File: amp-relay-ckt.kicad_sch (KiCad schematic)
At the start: 15 parts, among them K1 HK19F-DCxxV-SHC, K11 HK19F-DCxxV-SHC, Q2 Q_PNP_BCE, Q5 BSS123, U1 LM7805_TO220

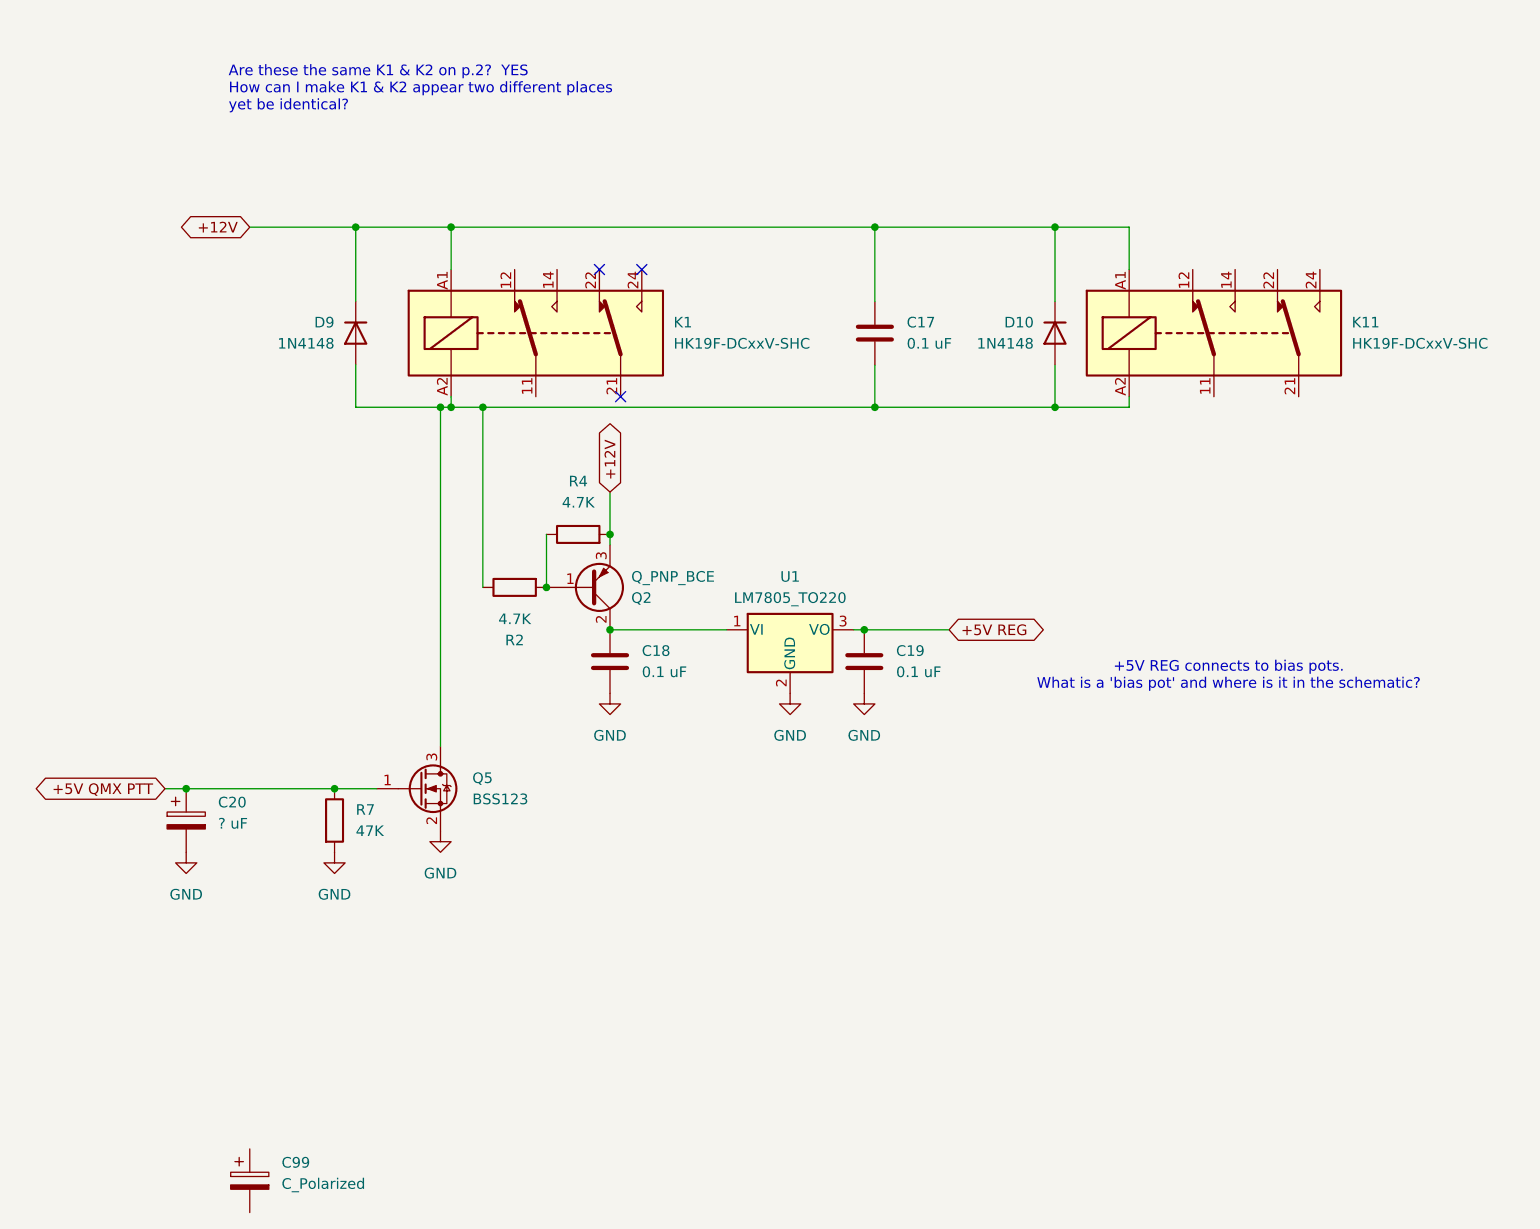
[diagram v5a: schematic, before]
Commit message: changed +5V and +12V from global symbol to the more normal voltage busses
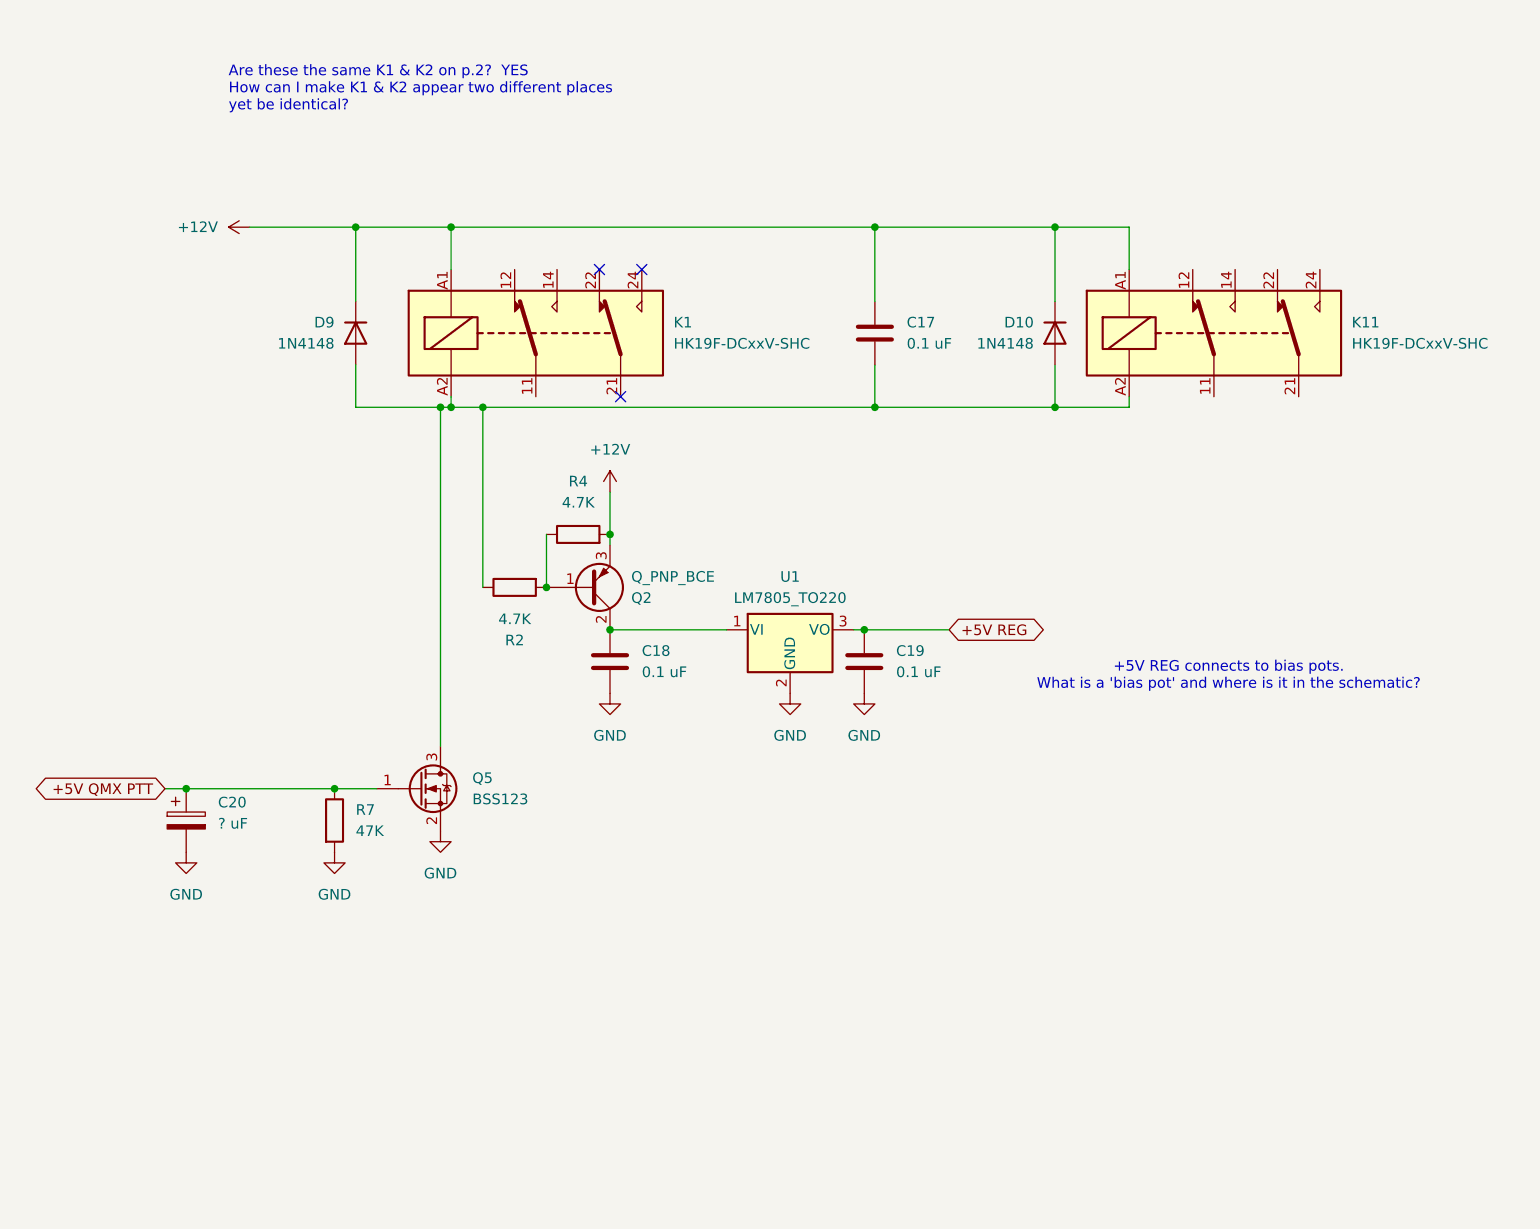
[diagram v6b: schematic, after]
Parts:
- removed C99: C_Polarized, symbol Device:C_Polarized
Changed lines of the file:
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@@
 		)
 	)
-	(global_label "+12V"
+	(global_label "+5V REG"
 		(shape bidirectional)
-		(at 102.87 85.09 90)
+		(at 143.51 101.6 0)
 		(fields_autoplaced yes)
 		(effects
@@
 		)
 		(property "Intersheetrefs" "${INTERSHEET_REFS}"
-			(at 102.87 75.9137 90)
-			(effects
-				(font
-					(size 1.27 1.27)
-				)
-				(justify left)
-				(hide yes)
-			)
-		)
-	)
-	(global_label "+5V REG"
+			(at 156.1334 101.6 0)
+			(effects
+				(font
+					(size 1.27 1.27)
+				)
+				(justify left)
+				(hide yes)
+			)
+		)
+	)
+	(global_label "+5V QMX PTT"
 		(shape bidirectional)
-		(at 143.51 101.6 0)
+		(at 49.53 120.65 180)
 		(fields_autoplaced yes)
 		(effects
@@
 				(size 1.27 1.27)
 			)
-			(justify left)
-		)
-		(property "Intersheetrefs" "${INTERSHEET_REFS}"
-			(at 156.1334 101.6 0)
-			(effects
-				(font
-					(size 1.27 1.27)
-				)
-				(justify left)
-				(hide yes)
-			)
-		)
-	)
-	(global_label "+5V QMX PTT"
-		(shape bidirectional)
-		(at 49.53 120.65 180)
-		(fields_autoplaced yes)
-		(effects
-			(font
-				(size 1.27 1.27)
-			)
 			(justify right)
 		)
@@
 				(justify right)
 				(hide yes)
-			)
-		)
-	)
-	(global_label "+12V"
-		(shape bidirectional)
-		(at 59.69 53.34 180)
-		(fields_autoplaced yes)
-		(effects
-			(font
-				(size 1.27 1.27)
-			)
-			(justify right)
-		)
-		(property "Intersheetrefs" "${INTERSHEET_REFS}"
-			(at 50.5137 53.34 0)
-			(effects
-				(font
-					(size 1.27 1.27)
-				)
-				(justify right)
-				(hide yes)
-			)
-		)
-	)
-	(symbol
-		(lib_id "Device:C_Polarized")
-		(at 59.69 167.64 0)
-		(unit 1)
-		(exclude_from_sim no)
-		(in_bom yes)
-		(on_board yes)
-		(dnp no)
-		(fields_autoplaced yes)
-		(property "Reference" "C99"
-			(at 63.5 165.4809 0)
-			(effects
-				(font
-					(size 1.27 1.27)
-				)
-				(justify left)
-			)
-		)
-		(property "Value" "C_Polarized"
-			(at 63.5 168.0209 0)
-			(effects
-				(font
-					(size 1.27 1.27)
-				)
-				(justify left)
-			)
-		)
-		(property "Footprint" ""
-			(at 60.6552 171.45 0)
-			(effects
-				(font
-					(size 1.27 1.27)
-				)
-				(hide yes)
-			)
-		)
-		(property "Datasheet" "~"
-			(at 59.69 167.64 0)
-			(effects
-				(font
-					(size 1.27 1.27)
-				)
-				(hide yes)
-			)
-		)
-		(property "Description" "Polarized capacitor"
-			(at 59.69 167.64 0)
-			(effects
-				(font
-					(size 1.27 1.27)
-				)
-				(hide yes)
-			)
-		)
-		(pin "2"
-		)
-		(pin "1"
-		)
-		(instances
-			(project ""
-				(path "/e63e39d7-6ac0-4ffd-8aa3-1841a4541b55/6e8a5723-6162-4126-acdf-190058cf1f27"
-					(reference "C99")
-					(unit 1)
-				)
 			)
 		)
@@
 	)
 	(symbol
+		(lib_id "power:+12V")
+		(at 59.69 53.34 90)
+		(unit 1)
+		(exclude_from_sim no)
+		(in_bom yes)
+		(on_board yes)
+		(dnp no)
+		(fields_autoplaced yes)
+		(property "Reference" "#PWR032"
+			(at 63.5 53.34 0)
+			(effects
+				(font
+					(size 1.27 1.27)
+				)
+				(hide yes)
+			)
+		)
+		(property "Value" "+12V"
+			(at 55.88 53.3399 90)
+			(effects
+				(font
+					(size 1.27 1.27)
+				)
+				(justify left)
+			)
+		)
+		(property "Footprint" ""
+			(at 59.69 53.34 0)
+			(effects
+				(font
+					(size 1.27 1.27)
+				)
+				(hide yes)
+			)
+		)
+		(property "Datasheet" ""
+			(at 59.69 53.34 0)
+			(effects
+				(font
+					(size 1.27 1.27)
+				)
+				(hide yes)
+			)
+		)
+		(property "Description" "Power symbol creates a global label with name \"+12V\""
+			(at 59.69 53.34 0)
+			(effects
+				(font
+					(size 1.27 1.27)
+				)
+				(hide yes)
+			)
+		)
+		(pin "1"
+		)
+		(instances
+			(project ""
+				(path "/e63e39d7-6ac0-4ffd-8aa3-1841a4541b55/6e8a5723-6162-4126-acdf-190058cf1f27"
+					(reference "#PWR032")
+					(unit 1)
+				)
+			)
+		)
+	)
+	(symbol
 		(lib_id "Device:D")
 		(at 72.39 66.04 90)
@@
 					(unit 1)
 				)
+			)
+		)
+	)
+	(symbol
+		(lib_id "power:+12V")
+		(at 102.87 85.09 0)
+		(unit 1)
+		(exclude_from_sim no)
+		(in_bom yes)
+		(on_board yes)
+		(dnp no)
+		(fields_autoplaced yes)
+		(property "Reference" "#PWR031"
+			(at 102.87 88.9 0)
+			(effects
+				(font
+					(size 1.27 1.27)
+				)
+				(hide yes)
+			)
+		)
+		(property "Value" "+12V"
+			(at 102.87 80.01 0)
+			(effects
+				(font
+					(size 1.27 1.27)
+				)
+			)
+		)
+		(property "Footprint" ""
+			(at 102.87 85.09 0)
+			(effects
+				(font
+					(size 1.27 1.27)
+				)
+				(hide yes)
+			)
+		)
+		(property "Datasheet" ""
+			(at 102.87 85.09 0)
+			(effects
+				(font
+					(size 1.27 1.27)
+				)
+				(hide yes)
+			)
+		)
+		(property "Description" "Power symbol creates a global label with name \"+12V\""
+			(at 102.87 85.09 0)
+			(effects
+				(font
+					(size 1.27 1.27)
+				)
+				(hide yes)
+			)
+		)
+		(pin "1"
+		)
+		(instances
+			(project ""
+				(path "/e63e39d7-6ac0-4ffd-8aa3-1841a4541b55/6e8a5723-6162-4126-acdf-190058cf1f27"
+					(reference "#PWR031")
+					(unit 1)
+				)

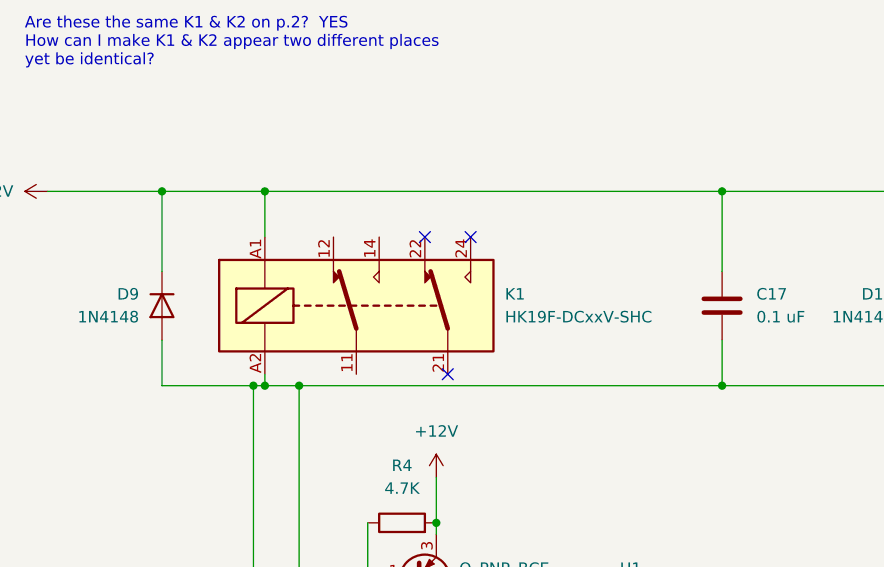
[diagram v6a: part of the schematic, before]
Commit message: could not figure out how to have two instances of K1 so I used global labels.  STINKY HACK
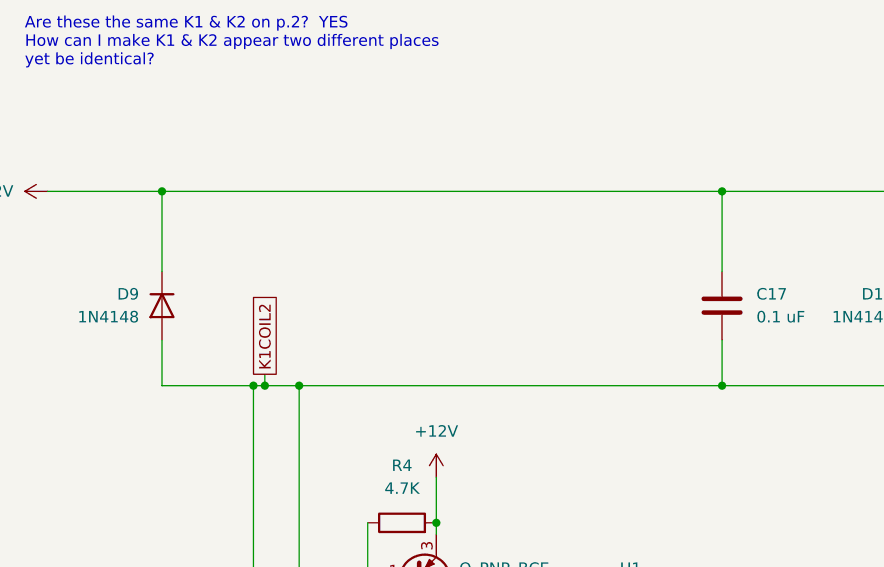
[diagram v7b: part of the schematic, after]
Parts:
- removed K1: HK19F-DCxxV-SHC, Relay_THT:Relay_DPDT_Finder_30.22, symbol Relay:HK19F-DCxxV-SHC
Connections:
- net K1COIL2: now reaches C17.2, D10.2 (A), D9.2 (A), K11.A2, Q5.3 (D), R2.1
- no-connect marks 3 -> 0
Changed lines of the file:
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@@
-	)
-	(junction
-		(at 83.82 53.34)
-		(diameter 0)
-		(color 0 0 0 0)
 	)
 	(junction
@@
 		(color 0 0 0 0)
 	)
-	(no_connect
-		(at 101.6 58.42)
-	)
-	(no_connect
-		(at 106.68 58.42)
-	)
-	(no_connect
-		(at 104.14 73.66)
-	)
 	(wire
 		(pts
@@
 	(wire
 		(pts
-			(xy 72.39 53.34) (xy 83.82 53.34)
+			(xy 72.39 53.34) (xy 134.62 53.34)
 		)
 		(stroke
@@
 	(wire
 		(pts
-			(xy 83.82 53.34) (xy 83.82 58.42)
-		)
-		(stroke
-			(width 0)
-			(type default)
-		)
-	)
-	(wire
-		(pts
 			(xy 133.35 101.6) (xy 132.08 101.6)
 		)
@@
 		(pts
 			(xy 83.82 73.66) (xy 83.82 74.93)
-		)
-		(stroke
-			(width 0)
-			(type default)
-		)
-	)
-	(wire
-		(pts
-			(xy 83.82 53.34) (xy 134.62 53.34)
 		)
 		(stroke
@@
 		)
 	)
+	(global_label "K1COIL2"
+		(shape passive)
+		(at 83.82 73.66 90)
+		(fields_autoplaced yes)
+		(effects
+			(font
+				(size 1.27 1.27)
+			)
+			(justify left)
+		)
+		(property "Intersheetrefs" "${INTERSHEET_REFS}"
+			(at 83.82 63.6733 90)
+			(effects
+				(font
+					(size 1.27 1.27)
+				)
+				(justify left)
+				(hide yes)
+			)
+		)
+	)
 	(global_label "+5V QMX PTT"
 		(shape bidirectional)
@@
 					(unit 1)
 				)
-			)
-		)
-	)
-	(symbol
-		(lib_id "Relay:HK19F-DCxxV-SHC")
-		(at 93.98 66.04 0)
-		(unit 1)
-		(exclude_from_sim no)
-		(in_bom yes)
-		(on_board yes)
-		(dnp no)
-		(fields_autoplaced yes)
-		(property "Reference" "K1"
-			(at 110.49 64.7699 0)
-			(effects
-				(font
-					(size 1.27 1.27)
-				)
-				(justify left)
-			)
-		)
-		(property "Value" "HK19F-DCxxV-SHC"
-			(at 110.49 67.3099 0)
-			(effects
-				(font
-					(size 1.27 1.27)
-				)
-				(justify left)
-			)
-		)
-		(property "Footprint" "Relay_THT:Relay_DPDT_Finder_30.22"
-			(at 76.2 78.74 0)
-			(effects
-				(font
-					(size 1.27 1.27)
-				)
-				(justify left)
-				(hide yes)
-			)
-		)
-		(property "Datasheet" "https://www.lcsc.com/datasheet/lcsc_datasheet_1810201512_Ningbo-Keke-New-Era-Appliance-HK19F-DC12V-SHG_C42803.pdf"
-			(at 93.98 83.82 0)
-			(effects
-				(font
-					(size 1.27 1.27)
-				)
-				(hide yes)
-			)
-		)
-		(property "Description" "HuiKe 19F monostable relay, DPDT, 1A"
-			(at 95.25 81.28 0)
-			(effects
-				(font
-					(size 1.27 1.27)
-				)
-				(hide yes)
-			)
-		)
-		(pin "A2"
-		)
-		(pin "A1"
-		)
-		(pin "22"
-		)
-		(pin "21"
-		)
-		(pin "24"
-		)
-		(pin "14"
-		)
-		(pin "12"
-		)
-		(pin "11"
-		)
-		(instances
-			(project "QMX-amp"
-				(path "/e63e39d7-6ac0-4ffd-8aa3-1841a4541b55/6e8a5723-6162-4126-acdf-190058cf1f27"
-					(reference "K1")
-					(unit 1)
-				)
